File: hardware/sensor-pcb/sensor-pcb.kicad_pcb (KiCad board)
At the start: 4 copper layers, 57 x 33 mm, 69 parts, among them J1 Conn_ARM_SWD_TagConnect_TC2030, J2 S5B-PH-SM4-TB, J4 S4B-PH-SM4-TB, Q1 BSS138BKSH, SW1 SKRKAHE020, SW2 SKRKAHE020, U1 STM32L476RCTx, U2 AP7354-33W5-7, U4 AP7354-33W5-7

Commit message: Deleted JR200 trimmer library with annoying license. Replaced with custom library. Updated licensing info.
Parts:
- C15: value C_Trim -> JR030; footprint JR200:CAPV_JR200 -> JRx-trimmer:JRx-trimmer
- C16: value 10pF -> 1pF
- moved C15 0.12 mm to (140.5, 99.2), turned to -90 degrees
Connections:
- C15 pad 1: /A_INTGR_INV -> /A_INTGR_OUT
- C15 pad 2: /A_INTGR_OUT -> /A_INTGR_INV
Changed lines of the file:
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@@
 		(sheetname "/")
 		(sheetfile "sensor-pcb.kicad_sch")
-		(attr exclude_from_pos_files)
+		(attr exclude_from_pos_files exclude_from_bom)
 		(fp_circle
 			(center 0 0)
@@
 		(sheetname "/")
 		(sheetfile "sensor-pcb.kicad_sch")
-		(attr exclude_from_pos_files)
+		(attr exclude_from_pos_files exclude_from_bom)
 		(fp_circle
 			(center 0 0)
@@
 		)
 	)
-	(footprint "JR200:CAPV_JR200"
-		(layer "F.Cu")
-		(at 140.5 99.3 90)
-		(property "Reference" "C15"
-			(at 3 0 180)
-			(layer "F.SilkS")
-			(effects
-				(font
-					(size 0.762 0.762)
-					(thickness 0.15)
-				)
-			)
-		)
-		(property "Value" "C_Trim"
-			(at 1.614 2.4064 90)
-			(layer "F.Fab")
-			(hide yes)
-			(effects
-				(font
-					(size 0.64 0.64)
-					(thickness 0.15)
-				)
-			)
-		)
-		(property "Datasheet" "~"
-			(at 0 0 90)
-			(layer "F.Fab")
-			(hide yes)
-			(effects
-				(font
-					(size 1.27 1.27)
-					(thickness 0.15)
-				)
-			)
-		)
-		(property "Description" "Trimmable capacitor"
-			(at 0 0 90)
-			(layer "F.Fab")
-			(hide yes)
-			(effects
-				(font
-					(size 1.27 1.27)
-					(thickness 0.15)
-				)
-			)
-		)
-		(sheetname "/")
-		(sheetfile "sensor-pcb.kicad_sch")
-		(attr smd)
-		(fp_line
-			(start -1.3 -1.55)
-			(end 1.75 -1.55)
-			(stroke
-				(width 0.127)
-				(type solid)
-			)
-			(layer "F.SilkS")
-		)
-		(fp_line
-			(start 1.75 -1.22)
-			(end 1.75 -1.55)
-			(stroke
-				(width 0.127)
-				(type solid)
-			)
-			(layer "F.SilkS")
-		)
-		(fp_line
-			(start -1.632 -1.219)
-			(end -1.3 -1.55)
-			(stroke
-				(width 0.127)
-				(type solid)
-			)
-			(layer "F.SilkS")
-		)
-		(fp_line
-			(start 1.75 1.55)
-			(end 1.75 1.22)
-			(stroke
-				(width 0.127)
-				(type solid)
-			)
-			(layer "F.SilkS")
-		)
-		(fp_line
-			(start 1.75 1.55)
-			(end -1.3 1.55)
-			(stroke
-				(width 0.127)
-				(type solid)
-			)
-			(layer "F.SilkS")
-		)
-		(fp_line
-			(start -1.3 1.55)
-			(end -1.632 1.219)
-			(stroke
-				(width 0.127)
-				(type solid)
-			)
-			(layer "F.SilkS")
-		)
-		(fp_line
-			(start 2.45 -1.8)
-			(end -2 -1.8)
-			(stroke
-				(width 0.05)
-				(type solid)
-			)
-			(layer "F.CrtYd")
-		)
-		(fp_line
-			(start -2 -1.8)
-			(end -2.45 -1.35)
-			(stroke
-				(width 0.05)
-				(type solid)
-			)
-			(layer "F.CrtYd")
-		)
-		(fp_line
-			(start -2.45 -1.35)
-			(end -2.45 1.35)
-			(stroke
-				(width 0.05)
-				(type solid)
-			)
-			(layer "F.CrtYd")
-		)
-		(fp_line
-			(start -2.45 1.35)
-			(end -2 1.8)
-			(stroke
-				(width 0.05)
-				(type solid)
-			)
-			(layer "F.CrtYd")
-		)
-		(fp_line
-			(start 2.45 1.8)
-			(end 2.45 -1.8)
-			(stroke
-				(width 0.05)
-				(type solid)
-			)
-			(layer "F.CrtYd")
-		)
-		(fp_line
-			(start -2 1.8)
-			(end 2.45 1.8)
-			(stroke
-				(width 0.05)
-				(type solid)
-			)
-			(layer "F.CrtYd")
-		)
-		(fp_line
-			(start 1.75 -1.55)
-			(end 1.75 1.55)
-			(stroke
-				(width 0.127)
-				(type solid)
-			)
-			(layer "F.Fab")
-		)
-		(fp_line
-			(start -1.3 -1.55)
-			(end 1.75 -1.55)
-			(stroke
-				(width 0.127)
-				(type solid)
-			)
-			(layer "F.Fab")
-		)
-		(fp_line
-			(start -1.75 -1.1)
-			(end -1.3 -1.55)
-			(stroke
-				(width 0.127)
-				(type solid)
-			)
-			(layer "F.Fab")
-		)
-		(fp_line
-			(start -1.75 1.1)
-			(end -1.75 -1.1)
-			(stroke
-				(width 0.127)
-				(type solid)
-			)
-			(layer "F.Fab")
-		)
-		(fp_line
-			(start 1.75 1.55)
-			(end -1.3 1.55)
-			(stroke
-				(width 0.127)
-				(type solid)
-			)
-			(layer "F.Fab")
-		)
-		(fp_line
-			(start -1.3 1.55)
-			(end -1.75 1.1)
-			(stroke
-				(width 0.127)
-				(type solid)
-			)
-			(layer "F.Fab")
-		)
-		(pad "1" smd rect
-			(at -1.7 0 90)
-			(size 1 1.8)
-			(layers "F.Cu" "F.Mask" "F.Paste")
-			(net 30 "/A_INTGR_INV")
-			(pintype "passive")
-			(solder_mask_margin 0.102)
-		)
-		(pad "2" smd rect
-			(at 1.7 0 90)
-			(size 1 1.8)
-			(layers "F.Cu" "F.Mask" "F.Paste")
-			(net 31 "/A_INTGR_OUT")
-			(pintype "passive")
-			(solder_mask_margin 0.102)
-		)
-		(embedded_fonts no)
-		(model "${KIPRJMOD}/libraries/JR200/JR200.step"
-			(offset
-				(xyz 0 0 0)
-			)
-			(scale
-				(xyz 1 1 1)
-			)
-			(rotate
-				(xyz -90 -0 -0)
-			)
-		)
-	)
 	(footprint "Button_Switch_SMD:SW_Push_SPST_NO_Alps_SKRK"
 		(layer "F.Cu")
@@
 		)
 	)
+	(footprint "JRx-trimmer:JRx-trimmer"
+		(layer "F.Cu")
+		(at 140.462 99.187 -90)
+		(descr "Capacitor trimmer.")
+		(property "Reference" "C15"
+			(at -0.5 -3 270)
+			(unlocked yes)
+			(layer "F.SilkS")
+			(effects
+				(font
+					(size 1 1)
+					(thickness 0.1)
+				)
+			)
+		)
+		(property "Value" "JR030"
+			(at 0 3 270)
+			(unlocked yes)
+			(layer "F.Fab")
+			(effects
+				(font
+					(size 1 1)
+					(thickness 0.15)
+				)
+			)
+		)
+		(property "Datasheet" "https://www.knowlescapacitors.com/getattachment/727ef5bd-b9cf-4698-a84c-cd891d1f5273/JR-Series"
+			(at 0 0 270)
+			(unlocked yes)
+			(layer "F.Fab")
+			(hide yes)
+			(effects
+				(font
+					(size 1 1)
+					(thickness 0.15)
+				)
+			)
+		)
+		(property "Description" "Trimmable capacitor"
+			(at 0 0 270)
+			(unlocked yes)
+			(layer "F.Fab")
+			(hide yes)
+			(effects
+				(font
+					(size 1 1)
+					(thickness 0.15)
+				)
+			)
+		)
+		(sheetname "/")
+		(sheetfile "sensor-pcb.kicad_sch")
+		(attr smd)
+		(fp_line
+			(start 1.5 1.677)
+			(end -1.123 1.677)
+			(stroke
+				(width 0.1)
+				(type default)
+			)
+			(layer "F.SilkS")
+		)
+		(fp_line
+			(start -1.8 1)
+			(end -1.123 1.677)
+			(stroke
+				(width 0.1)
+				(type default)
+			)
+			(layer "F.SilkS")
+		)
+		(fp_line
+			(start 1.5 1)
+			(end 1.5 1.677)
+			(stroke
+				(width 0.1)
+				(type default)
+			)
+			(layer "F.SilkS")
+		)
+		(fp_line
+			(start -1.8 -1)
+			(end -1.123 -1.677)
+			(stroke
+				(width 0.1)
+				(type default)
+			)
+			(layer "F.SilkS")
+		)
+		(fp_line
+			(start 1.5 -1.677)
+			(end 1.5 -1)
+			(stroke
+				(width 0.1)
+				(type default)
+			)
+			(layer "F.SilkS")
+		)
+		(fp_line
+			(start 1.5 -1.677)
+			(end -1.123 -1.677)
+			(stroke
+				(width 0.1)
+				(type default)
+			)
+			(layer "F.SilkS")
+		)
+		(fp_line
+			(start -2.5 2)
+			(end 2.5 2)
+			(stroke
+				(width 0.05)
+				(type default)
+			)
+			(layer "F.CrtYd")
+		)
+		(fp_line
+			(start 2.5 2)
+			(end 2.5 -2)
+			(stroke
+				(width 0.05)
+				(type default)
+			)
+			(layer "F.CrtYd")
+		)
+		(fp_line
+			(start -2.5 -2)
+			(end -2.5 2)
+			(stroke
+				(width 0.05)
+				(type default)
+			)
+			(layer "F.CrtYd")
+		)
+		(fp_line
+			(start 2.5 -2)
+			(end -2.5 -2)
+			(stroke
+				(width 0.05)
+				(type default)
+			)
+			(layer "F.CrtYd")
+		)
+		(fp_text user "${REFERENCE}"
+			(at 0 4.5 270)
+			(unlocked yes)
+			(layer "F.Fab")
+			(effects
+				(font
+					(size 1 1)
+					(thickness 0.15)
+				)
+			)
+		)
+		(pad "1" smd roundrect
+			(at -1.7 0)
+			(size 1.8 1)
+			(layers "F.Cu" "F.Mask" "F.Paste")
+			(roundrect_rratio 0.15)
+			(net 31 "/A_INTGR_OUT")
+			(pintype "passive")
+		)
+		(pad "2" smd roundrect
+			(at 1.7 0)
+			(size 1.8 1)
+			(layers "F.Cu" "F.Mask" "F.Paste")
+			(roundrect_rratio 0.15)
+			(net 30 "/A_INTGR_INV")
+			(pintype "passive")
+		)
+		(embedded_fonts no)
+		(model "${KIPRJMOD}/libraries/jrx-trimmer/JR200.STEP"
+			(offset
+				(xyz 0 0 0)
+			)
+			(scale
+				(xyz 1 1 1)
+			)
+			(rotate
+				(xyz -90 -0 -0)
+			)
+		)
+	)
 	(footprint "Capacitor_SMD:C_0805_2012Metric"
 		(layer "F.Cu")
@@
 			)
 		)
-		(property "Value" "10pF"
+		(property "Value" "1pF"
 			(at 0 1.16 90)
 			(layer "F.Fab")

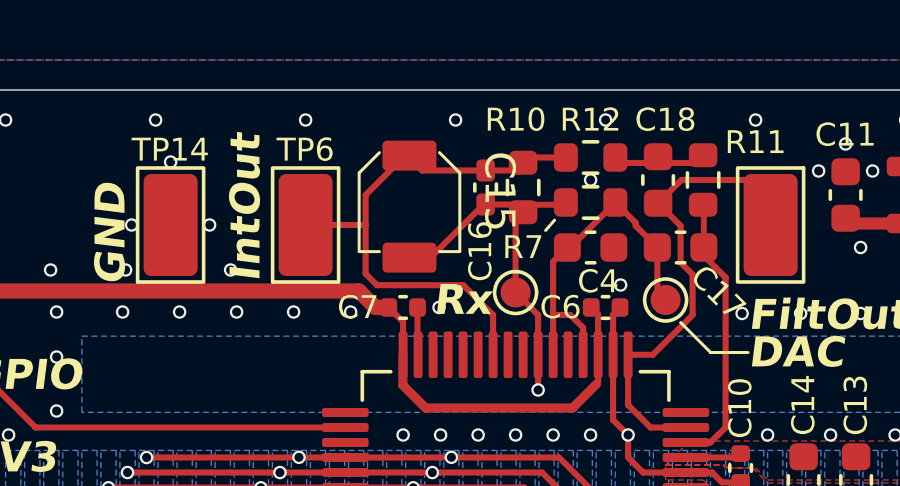
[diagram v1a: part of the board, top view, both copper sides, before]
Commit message: Reworked sensor-PCB schematic/layout output jobs
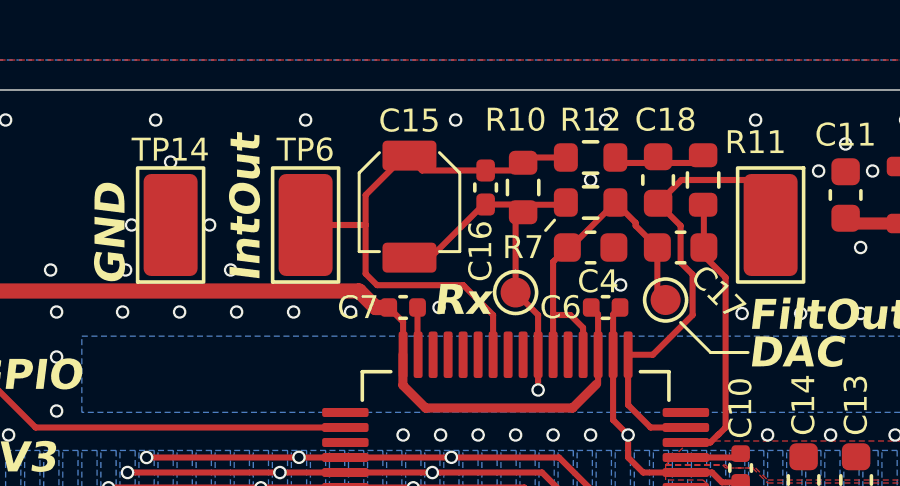
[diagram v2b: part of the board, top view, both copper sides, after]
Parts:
- D2: value APTD3216LSURCK -> APT3216LSECK/J3-PRV
- TP10, TP12, TP14, TP17, TP6, TP8: value TestPoint_Alt -> TP_Keystone_5015
